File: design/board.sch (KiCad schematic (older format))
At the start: 6 parts, among them IC1 ATTINY10-P, U1 NodeMCU1.0(ESP-12E), U2 BME280

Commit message: ws2812b Anschluss auf dem Schaltplan hinzugefügt
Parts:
- added P?: WS2812b, symbol CONN_01X03
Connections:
- net labels added: RX
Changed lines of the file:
@@
 LIBS:valves
 LIBS:ESP8266
+LIBS:board-cache
 EELAYER 25 0
 EELAYER END
@@
 Text GLabel 3800 2000 2    60   Input ~ 0
 D0
+$Comp
+L CONN_01X03 P?
+U 1 1 58F2695A
+P 4700 3950
+F 0 "P?" H 4700 4150 50  0000 C CNN
+F 1 "WS2812b" V 4800 3950 50  0000 C CNN
+F 2 "" H 4700 3950 50  0000 C CNN
+F 3 "" H 4700 3950 50  0000 C CNN
+	1    4700 3950
+	1    0    0    -1
+$EndComp
+Text GLabel 3800 3100 2    60   Input ~ 0
+RX
+Text GLabel 4500 3950 0    60   Input ~ 0
+RX
+$Comp
+L VCC #PWR?
+U 1 1 58F26B2C
+P 4500 3850
+F 0 "#PWR?" H 4500 3700 50  0001 C CNN
+F 1 "VCC" H 4500 4000 50  0000 C CNN
+F 2 "" H 4500 3850 50  0000 C CNN
+F 3 "" H 4500 3850 50  0000 C CNN
+	1    4500 3850
+	1    0    0    -1
+$EndComp
+$Comp
+L GND #PWR?
+U 1 1 58F26C1E
+P 4500 4050
+F 0 "#PWR?" H 4500 3800 50  0001 C CNN
+F 1 "GND" H 4500 3900 50  0000 C CNN
+F 2 "" H 4500 4050 50  0000 C CNN
+F 3 "" H 4500 4050 50  0000 C CNN
+	1    4500 4050
+	1    0    0    -1
+$EndComp
 $EndSCHEMATC

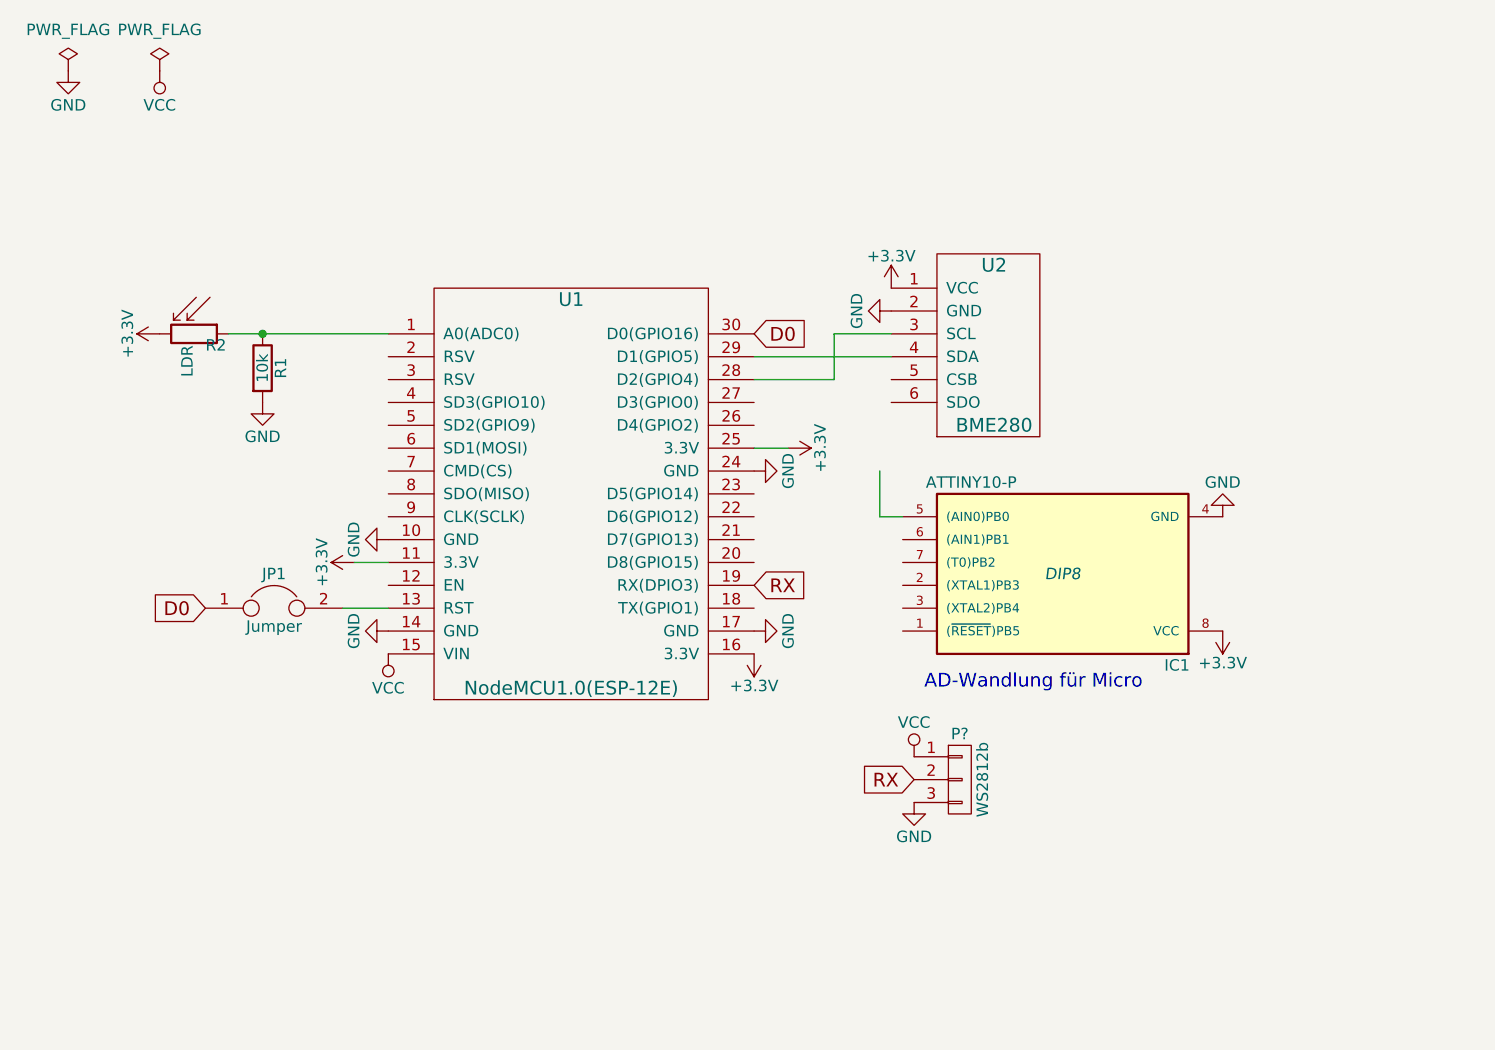
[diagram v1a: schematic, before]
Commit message: Schaltplan aktualisiert und erweitert
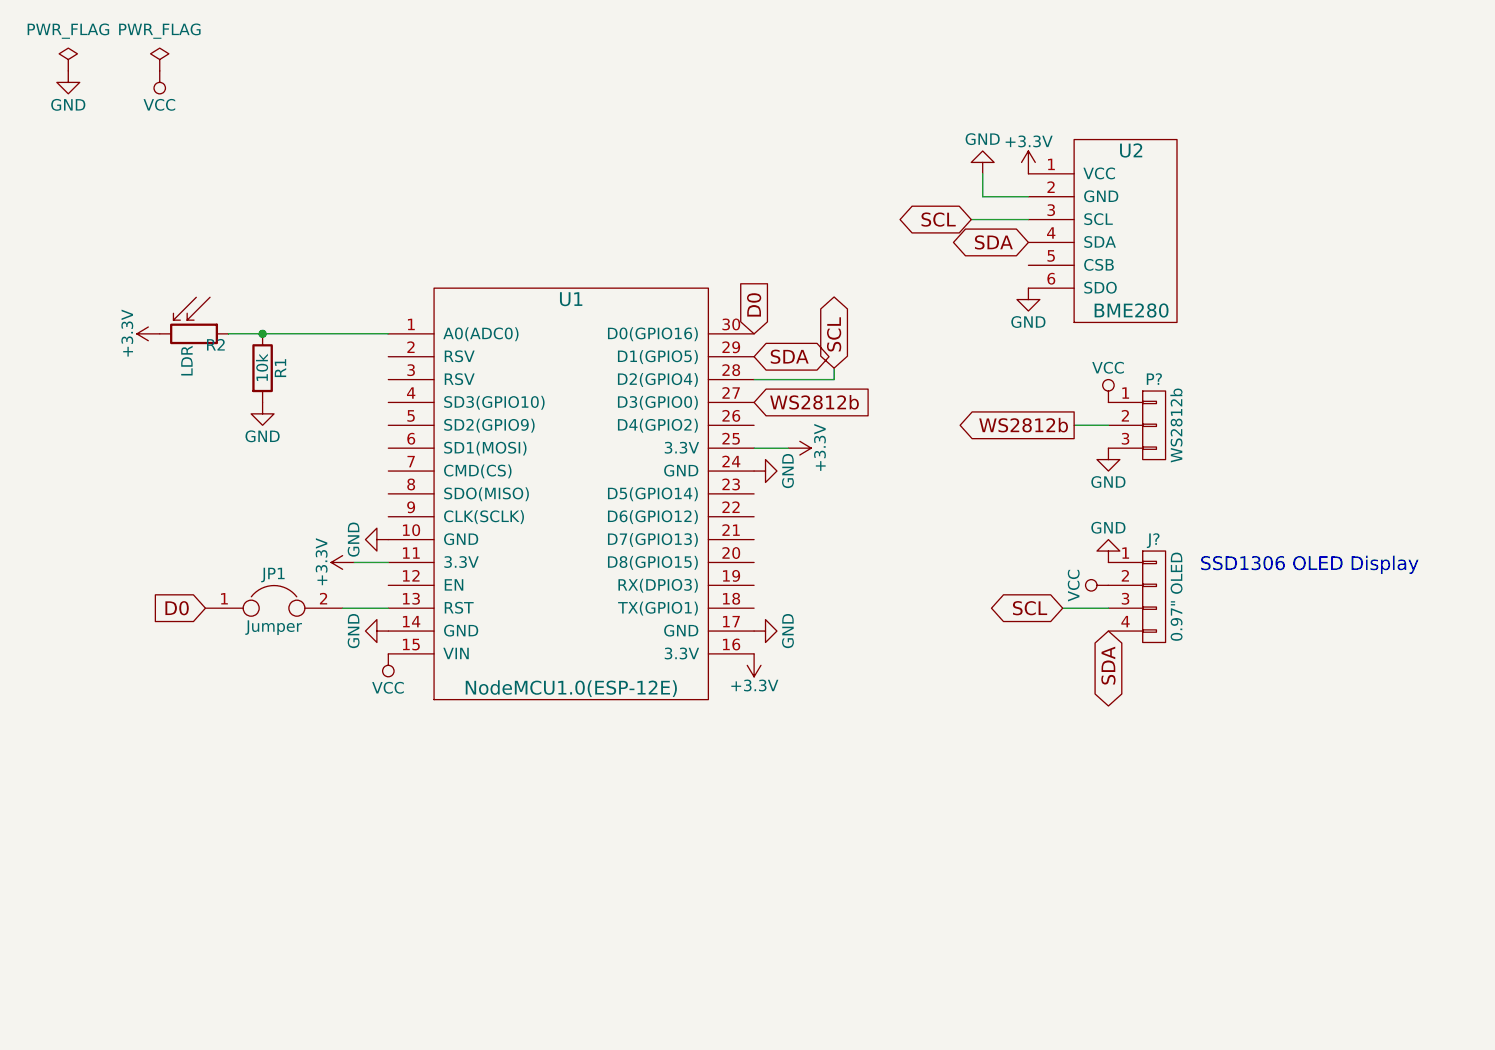
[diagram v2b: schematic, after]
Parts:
- removed IC1: ATTINY10-P, DIP8, symbol ATTINY10-P
- added J?: 0.97\" OLED, symbol CONN_01X04
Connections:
- net labels added: SCL, SDA, WS2812b
- net labels removed: RX
- wire segments 10 -> 11
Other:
- note added: "SSD1306 OLED Display"
- note removed: "AD-Wandlung für Micro"
- moved on the sheet: P?, U2
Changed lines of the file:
@@
-$EndComp
-$Comp
-L ATTINY10-P IC1
-U 1 1 58E9488E
-P 5150 3050
-F 0 "IC1" H 4650 3450 50  0000 C CNN
-F 1 "ATTINY10-P" H 5550 2650 50  0000 C CNN
-F 2 "DIP8" H 5150 3050 50  0000 C CIN
-F 3 "" H 5150 3050 50  0000 C CNN
-	1    5150 3050
-	-1   0    0    1
 $EndComp
 $Comp
 L BME280 U2
 U 1 1 58E966B6
-P 5450 2200
-F 0 "U2" H 4850 2700 60  0000 C CNN
-F 1 "BME280" H 4850 2000 60  0000 C CNN
-F 2 "" H 5300 2750 60  0001 C CNN
-F 3 "" H 5300 2750 60  0001 C CNN
-	1    5450 2200
+P 6050 1700
+F 0 "U2" H 5450 2200 60  0000 C CNN
+F 1 "BME280" H 5450 1500 60  0000 C CNN
+F 2 "" H 5900 2250 60  0001 C CNN
+F 3 "" H 5900 2250 60  0001 C CNN
+	1    6050 1700
 	1    0    0    -1
 $EndComp
@@
 L +3.3V #PWR13
 U 1 1 58E96994
-P 4400 1800
-F 0 "#PWR13" H 4400 1650 50  0001 C CNN
-F 1 "+3.3V" H 4400 1940 50  0000 C CNN
-F 2 "" H 4400 1800 50  0000 C CNN
-F 3 "" H 4400 1800 50  0000 C CNN
-	1    4400 1800
+P 5000 1300
+F 0 "#PWR13" H 5000 1150 50  0001 C CNN
+F 1 "+3.3V" H 5000 1440 50  0000 C CNN
+F 2 "" H 5000 1300 50  0000 C CNN
+F 3 "" H 5000 1300 50  0000 C CNN
+	1    5000 1300
 	1    0    0    -1
 $EndComp
@@
 L GND #PWR14
 U 1 1 58E969B2
-P 4400 1900
-F 0 "#PWR14" H 4400 1650 50  0001 C CNN
-F 1 "GND" H 4400 1750 50  0000 C CNN
-F 2 "" H 4400 1900 50  0000 C CNN
-F 3 "" H 4400 1900 50  0000 C CNN
-	1    4400 1900
-	0    1    1    0
-$EndComp
-$Comp
-L GND #PWR15
-U 1 1 58E97077
-P 5850 2800
-F 0 "#PWR15" H 5850 2550 50  0001 C CNN
-F 1 "GND" H 5850 2650 50  0000 C CNN
-F 2 "" H 5850 2800 50  0000 C CNN
-F 3 "" H 5850 2800 50  0000 C CNN
-	1    5850 2800
+P 4800 1300
+F 0 "#PWR14" H 4800 1050 50  0001 C CNN
+F 1 "GND" H 4800 1150 50  0000 C CNN
+F 2 "" H 4800 1300 50  0000 C CNN
+F 3 "" H 4800 1300 50  0000 C CNN
+	1    4800 1300
 	-1   0    0    1
 $EndComp
-$Comp
-L +3.3V #PWR16
-U 1 1 58E97095
-P 5850 3300
-F 0 "#PWR16" H 5850 3150 50  0001 C CNN
-F 1 "+3.3V" H 5850 3440 50  0000 C CNN
-F 2 "" H 5850 3300 50  0000 C CNN
-F 3 "" H 5850 3300 50  0000 C CNN
-	1    5850 3300
-	-1   0    0    1
-$EndComp
-Text Notes 5500 3560 2    60   ~ 0
-AD-Wandlung für Micro
 $Comp
 L Jumper JP1
@@
 	1500 2000 2200 2000
 Wire Wire Line
-	3800 2100 4400 2100
-Wire Wire Line
-	3800 2200 4150 2200
-Wire Wire Line
-	4150 2200 4150 2000
-Wire Wire Line
-	4150 2000 4400 2000
-Wire Wire Line
-	4450 2800 4350 2800
-Wire Wire Line
-	4350 2800 4350 2600
-Wire Wire Line
 	2000 3200 2200 3200
 Text GLabel 1400 3200 0    60   Input ~ 0
 D0
-Text GLabel 3800 2000 2    60   Input ~ 0
+Text GLabel 3800 2000 1    60   Input ~ 0
 D0
 $Comp
 L CONN_01X03 P?
 U 1 1 58F2695A
-P 4700 3950
-F 0 "P?" H 4700 4150 50  0000 C CNN
-F 1 "WS2812b" V 4800 3950 50  0000 C CNN
-F 2 "" H 4700 3950 50  0000 C CNN
-F 3 "" H 4700 3950 50  0000 C CNN
-	1    4700 3950
+P 5550 2400
+F 0 "P?" H 5550 2600 50  0000 C CNN
+F 1 "WS2812b" V 5650 2400 50  0000 C CNN
+F 2 "" H 5550 2400 50  0000 C CNN
+F 3 "" H 5550 2400 50  0000 C CNN
+	1    5550 2400
 	1    0    0    -1
 $EndComp
-Text GLabel 3800 3100 2    60   Input ~ 0
-RX
-Text GLabel 4500 3950 0    60   Input ~ 0
-RX
+Text GLabel 5200 2400 0    60   Output ~ 0
+WS2812b
 $Comp
 L VCC #PWR?
 U 1 1 58F26B2C
-P 4500 3850
-F 0 "#PWR?" H 4500 3700 50  0001 C CNN
-F 1 "VCC" H 4500 4000 50  0000 C CNN
-F 2 "" H 4500 3850 50  0000 C CNN
-F 3 "" H 4500 3850 50  0000 C CNN
-	1    4500 3850
+P 5350 2300
+F 0 "#PWR?" H 5350 2150 50  0001 C CNN
+F 1 "VCC" H 5350 2450 50  0000 C CNN
+F 2 "" H 5350 2300 50  0000 C CNN
+F 3 "" H 5350 2300 50  0000 C CNN
+	1    5350 2300
 	1    0    0    -1
 $EndComp
@@
 L GND #PWR?
 U 1 1 58F26C1E
-P 4500 4050
-F 0 "#PWR?" H 4500 3800 50  0001 C CNN
-F 1 "GND" H 4500 3900 50  0000 C CNN
-F 2 "" H 4500 4050 50  0000 C CNN
-F 3 "" H 4500 4050 50  0000 C CNN
-	1    4500 4050
+P 5350 2500
+F 0 "#PWR?" H 5350 2250 50  0001 C CNN
+F 1 "GND" H 5350 2350 50  0000 C CNN
+F 2 "" H 5350 2500 50  0000 C CNN
+F 3 "" H 5350 2500 50  0000 C CNN
+	1    5350 2500
 	1    0    0    -1
 $EndComp
+Text GLabel 3800 2300 2    60   Input ~ 0
+WS2812b
+Wire Wire Line
+	5200 2400 5350 2400
+$Comp
+L GND #PWR?
+U 1 1 590CCC6B
+P 5000 1800
+F 0 "#PWR?" H 5000 1550 50  0001 C CNN
+F 1 "GND" H 5000 1650 50  0000 C CNN
+F 2 "" H 5000 1800 50  0001 C CNN
+F 3 "" H 5000 1800 50  0001 C CNN
+	1    5000 1800
+	1    0    0    -1
+$EndComp
+Text GLabel 3800 2100 2    60   BiDi ~ 0
+SDA
+Text GLabel 4150 2150 1    60   BiDi ~ 0
+SCL
+Text GLabel 4750 1500 0    60   BiDi ~ 0
+SCL
+Wire Wire Line
+	4750 1500 5000 1500
+Text GLabel 5000 1600 0    60   BiDi ~ 0
+SDA
+Wire Wire Line
+	5000 1400 4800 1400
+Wire Wire Line
+	4800 1400 4800 1300
+Wire Wire Line
+	3800 2200 4150 2200
+Wire Wire Line
+	4150 2200 4150 2150
+$Comp
+L CONN_01X04 J?
+U 1 1 590CE438
+P 5550 3150
+F 0 "J?" H 5550 3400 50  0000 C CNN
+F 1 "0.97\" OLED" V 5650 3150 50  0000 C CNN
+F 2 "" H 5550 3150 50  0001 C CNN
+F 3 "" H 5550 3150 50  0001 C CNN
+	1    5550 3150
+	1    0    0    -1
+$EndComp
+$Comp
+L GND #PWR?
+U 1 1 590CE4E4
+P 5350 3000
+F 0 "#PWR?" H 5350 2750 50  0001 C CNN
+F 1 "GND" H 5350 2850 50  0000 C CNN
+F 2 "" H 5350 3000 50  0001 C CNN
+F 3 "" H 5350 3000 50  0001 C CNN
+	1    5350 3000
+	-1   0    0    1
+$EndComp
+$Comp
+L VCC #PWR?
+U 1 1 590CE506
+P 5350 3100
+F 0 "#PWR?" H 5350 2950 50  0001 C CNN
+F 1 "VCC" H 5350 3250 50  0000 C CNN
+F 2 "" H 5350 3100 50  0001 C CNN
+F 3 "" H 5350 3100 50  0001 C CNN
+	1    5350 3100
+	0    -1   -1   0
+$EndComp
+Text GLabel 5150 3200 0    60   BiDi ~ 0
+SCL
+Wire Wire Line
+	5150 3200 5350 3200
+Text GLabel 5350 3300 3    60   BiDi ~ 0
+SDA
+Text Notes 5750 3050 0    60   ~ 0
+SSD1306 OLED Display
 $EndSCHEMATC

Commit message: modified and refresched
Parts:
- removed JP1: Jumper, symbol Jumper
- removed R1: 10k, symbol R
- removed R2: LDR, symbol R_PHOTO
- added J?: CONN_01X02, symbol CONN_01X02
- added J?: CONN_01X06, symbol CONN_01X06
- added JP? (x2): Jumper_NC_Dual, symbol Jumper_NC_Dual
- added LS?: Speaker, symbol Speaker
- added M?: Mic, symbol CONN_01X03
- added R?: 10K, symbol R
- added SW?: SW_Push, symbol SW_Push
- gave numbers to parts that had none: 1
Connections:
- net labels added: MIC, SD3
- wire segments 11 -> 29
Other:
- moved on the sheet: C?, P?

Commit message: finalizing PCB Layout
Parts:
- removed J?: CONN_01X06, symbol CONN_01X06
- added C1: 2200µF, Capacitors_THT:CP_Radial_D10.0mm_P2.50mm, symbol CP
- added D1: D, Diodes_THT:D_DO-201AD_P15.24mm_Horizontal, symbol D
- added J2: DEBUG_CONN, Socket_Strips:Socket_Strip_Straight_1x07_Pitch2.54mm, symbol CONN_01X07
- J1: renamed from M?; footprint (none) -> Socket_Strips:Socket_Strip_Straight_1x03_Pitch2.54mm
- J3: renamed from J?; value CONN_01X02 -> PWR_CONN; footprint (none) -> Pin_Headers:Pin_Header_Straight_1x02_Pitch2.54mm
- J4: renamed from C?; footprint (none) -> Socket_Strips:Socket_Strip_Straight_1x04_Pitch2.54mm
- J5: renamed from P?; footprint (none) -> Socket_Strips:Socket_Strip_Straight_1x03_Pitch2.54mm
- JP1: renamed from JP?; value Jumper_NC_Dual -> DSLEEP_JUMP; footprint (none) -> Pin_Headers:Pin_Header_Straight_1x03_Pitch2.54mm
- JP2: renamed from JP?; value Jumper_NC_Dual -> BEEPER_JUMP; footprint (none) -> Pin_Headers:Pin_Header_Straight_1x03_Pitch2.54mm
- LS1: renamed from LS?; footprint (none) -> Buzzers_Beepers:MagneticBuzzer_ProSignal_ABT-410-RC
- R1: renamed from R?; footprint (none) -> Resistors_THT:R_Axial_DIN0309_L9.0mm_D3.2mm_P12.70mm_Horizontal
- SW1: renamed from SW?; footprint (none) -> Pin_Headers:Pin_Header_Straight_1x02_Pitch2.54mm
- U1: footprint (none) -> ESP8266:NodeMCU1.0(12-E)
- U2: footprint (none) -> Socket_Strips:Socket_Strip_Straight_1x06_Pitch2.54mm
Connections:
- net labels added: +3V3
- wire segments 29 -> 38
- no-connect marks 0 -> 17
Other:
- moved on the sheet: R1
